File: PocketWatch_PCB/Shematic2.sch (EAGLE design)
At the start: 52 parts, among them IC1 74HC139D, Q1 BCX71SMD, Q2 BCX71SMD, Q3 BCX71SMD, Q4 BCX71SMD, Q5 BCX70SMD, Q6 BCX70SMD, Q7 BCX70SMD, Q8 BCX70SMD, U2 ATTINY88-AU

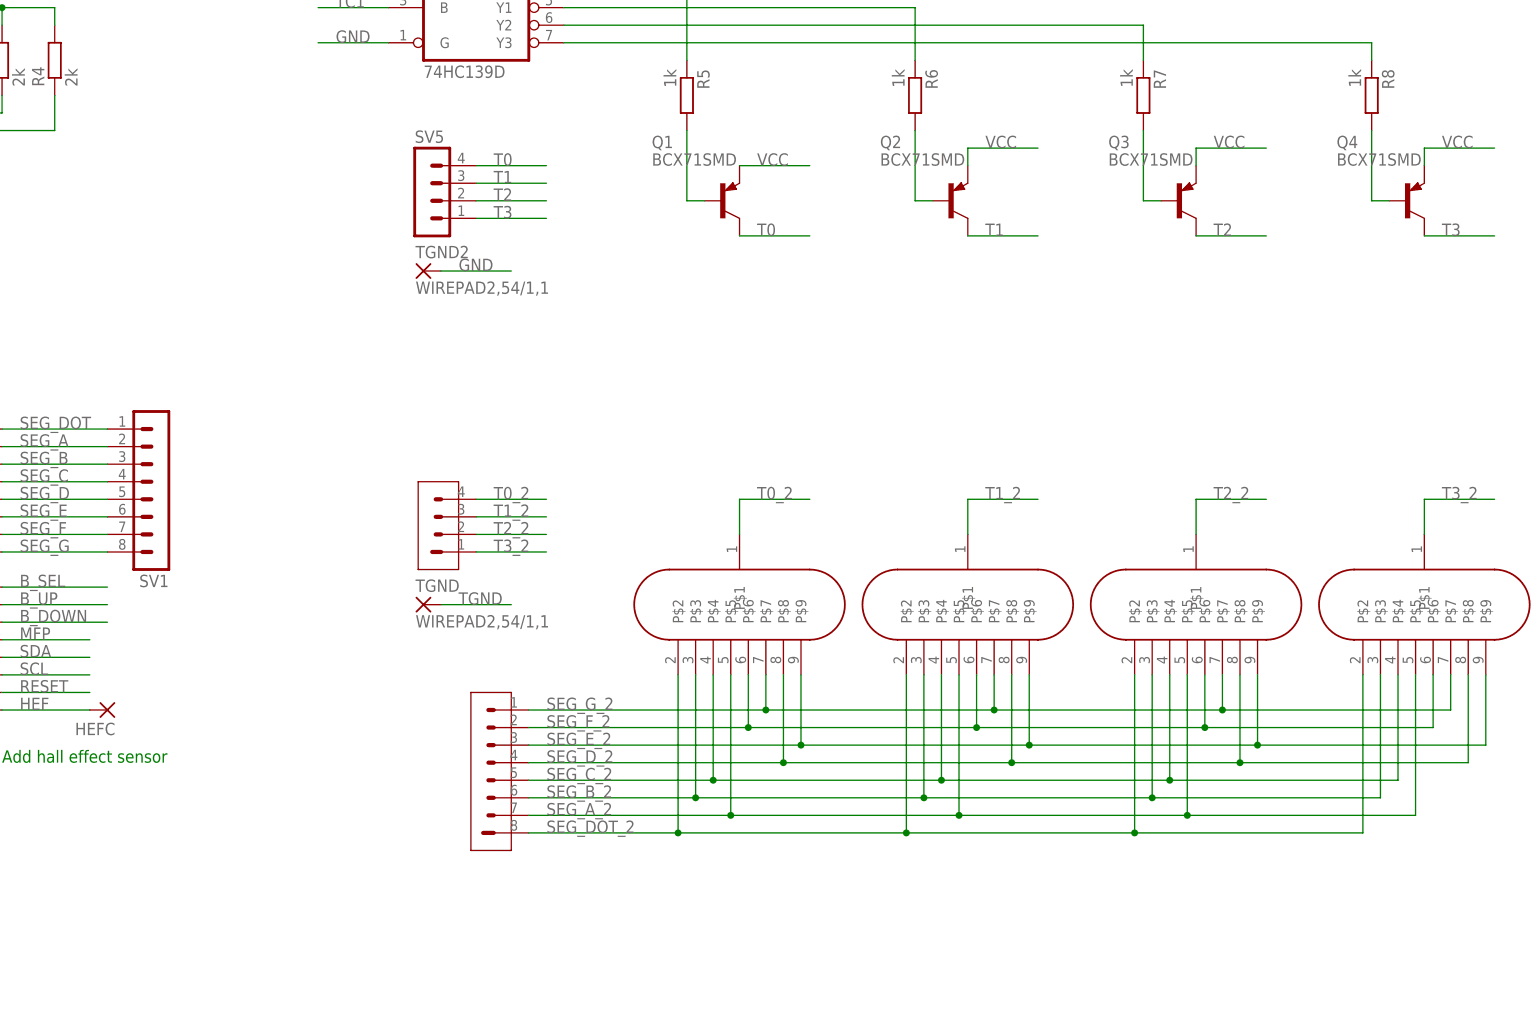
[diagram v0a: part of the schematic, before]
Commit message: Added second version of the board for attempted board optimization
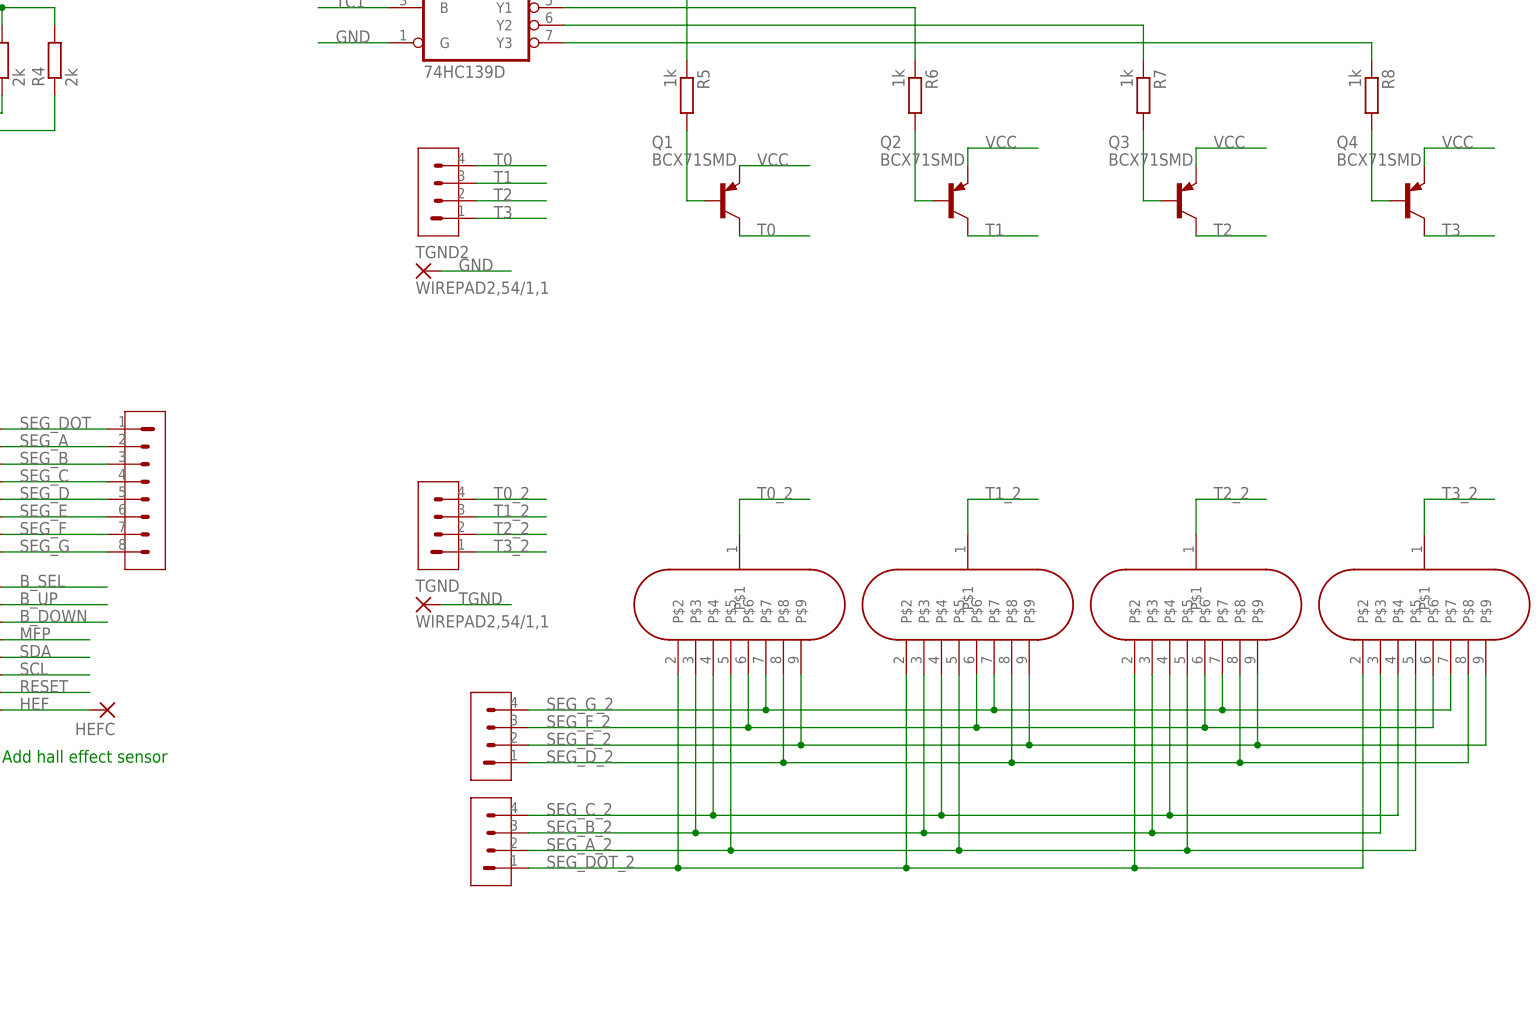
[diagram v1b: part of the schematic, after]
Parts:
- added SV7: H04, Library:H04
- SV1: value (none) -> H08; device con-lstb:MA08-1 -> Library:H08
- SV2: value H08 -> H04; device Library:H08 -> Library:H04
- SV5: value (none) -> H04; device con-lstb:MA04-1 -> Library:H04
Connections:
- net SEG_A_2: now also SV7.2; no longer SV2.2
- net SEG_B_2: now also SV7.3; no longer SV2.3
- net SEG_C_2: now also SV7.4; no longer SV2.4
- net SEG_DOT_2: now also SV7.1; no longer SV2.1
- net SEG_D_2: now also SV2.1; no longer SV2.5
- net SEG_E_2: now also SV2.2; no longer SV2.6
- net SEG_F_2: now also SV2.3; no longer SV2.7
- net SEG_G_2: now also SV2.4; no longer SV2.8
